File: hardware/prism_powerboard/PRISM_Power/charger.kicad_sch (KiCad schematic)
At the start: 23 parts, among them Q1 AO3400A, Q2 AO3400A, U2 BQ25895RTW, U3 BQ297xy

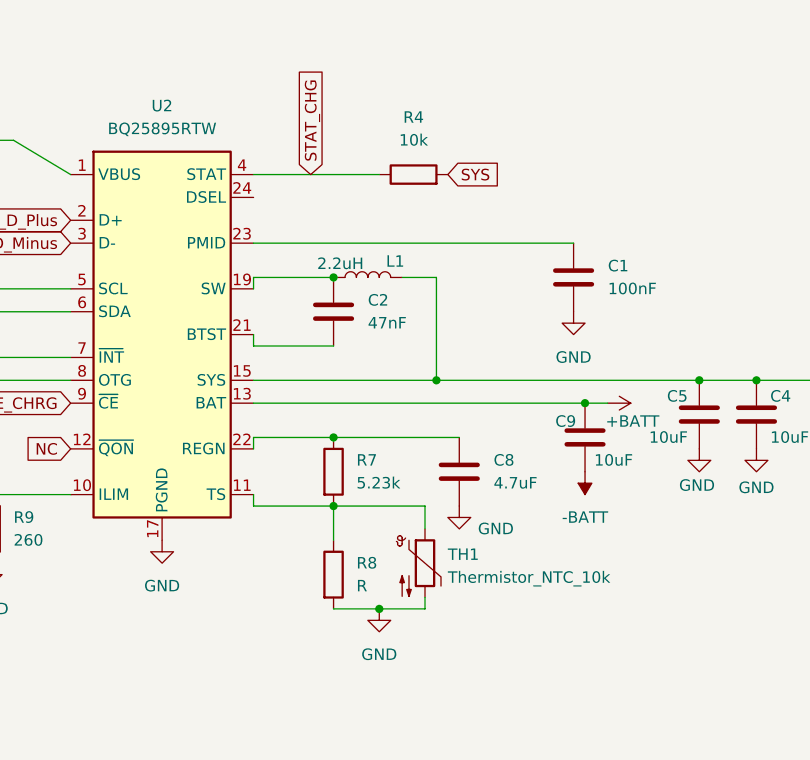
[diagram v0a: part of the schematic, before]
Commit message: Finished Schematics and Start Routing
Finished Schematics and started routing the PCB lines. Added and ensured all footprints were accurate
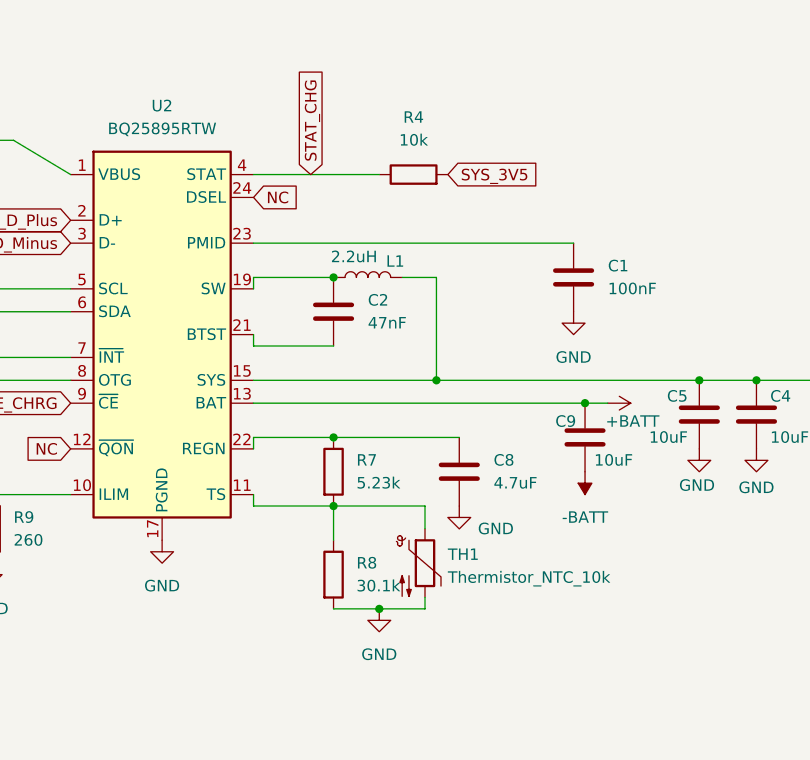
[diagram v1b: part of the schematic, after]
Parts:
- C1, C2, C3, C4, C5, C6, C8, C9: footprint (none) -> Capacitor_SMD:C_0805_2012Metric_Pad1.18x1.45mm_HandSolder
- L1: footprint (none) -> Inductor_SMD:L_0805_2012Metric_Pad1.05x1.20mm_HandSolder
- R10, R11, R2, R4, R5, R6, R7, R9: footprint (none) -> Resistor_SMD:R_0805_2012Metric_Pad1.20x1.40mm_HandSolder
- R8: value R -> 30.1k; footprint (none) -> Resistor_SMD:R_0805_2012Metric_Pad1.20x1.40mm_HandSolder
- TH1: footprint (none) -> Resistor_THT:R_Axial_DIN0204_L3.6mm_D1.6mm_P2.54mm_Vertical
- U2: footprint Package_DFN_QFN:Texas_RTW_WQFN-24-1EP_4x4mm_P0.5mm_EP2.7x2.7mm_ThermalVias -> BQ25895:RTW0024H
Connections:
- net NC: now also U2.24 (DSEL)
- net SYS: no longer R4.2
- new net SYS_3V5: R4.2
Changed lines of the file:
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@@
 		)
 	)
+	(global_label "NC"
+		(shape input)
+		(at 142.24 78.74 0)
+		(fields_autoplaced yes)
+		(effects
+			(font
+				(size 1.27 1.27)
+			)
+			(justify left)
+		)
+		(property "Intersheetrefs" "${INTERSHEET_REFS}"
+			(at 147.8257 78.74 0)
+			(hide yes)
+			(show_name no)
+			(do_not_autoplace no)
+			(effects
+				(font
+					(size 1.27 1.27)
+				)
+				(justify left)
+			)
+		)
+	)
 	(global_label "I2C_SCL_1V8"
 		(shape input)
@@
 		)
 	)
-	(global_label "SYS"
+	(global_label "SYS_3V5"
 		(shape input)
 		(at 163.83 76.2 0)
@@
 		)
 		(property "Intersheetrefs" "${INTERSHEET_REFS}"
-			(at 170.3228 76.2 0)
+			(at 174.798 76.2 0)
 			(hide yes)
 			(show_name no)
@@
 			)
 		)
-		(property "Footprint" ""
+		(property "Footprint" "Capacitor_SMD:C_0805_2012Metric_Pad1.18x1.45mm_HandSolder"
 			(at 39.0652 157.48 0)
 			(hide yes)
@@
 			)
 		)
-		(property "Footprint" ""
+		(property "Footprint" "Resistor_SMD:R_0805_2012Metric_Pad1.20x1.40mm_HandSolder"
 			(at 149.352 109.22 90)
 			(hide yes)
@@
 			)
 		)
-		(property "Footprint" ""
+		(property "Footprint" "Resistor_SMD:R_0805_2012Metric_Pad1.20x1.40mm_HandSolder"
 			(at 160.02 77.978 90)
 			(hide yes)
@@
 			)
 		)
-		(property "Footprint" ""
+		(property "Footprint" "Resistor_SMD:R_0805_2012Metric_Pad1.20x1.40mm_HandSolder"
 			(at 111.252 115.57 90)
 			(hide yes)
@@
 			)
 		)
-		(property "Footprint" ""
+		(property "Footprint" "Capacitor_SMD:C_0805_2012Metric_Pad1.18x1.45mm_HandSolder"
 			(at 107.6452 72.39 0)
 			(hide yes)
@@
 			)
 		)
-		(property "Footprint" ""
+		(property "Footprint" "Capacitor_SMD:C_0805_2012Metric_Pad1.18x1.45mm_HandSolder"
 			(at 199.0852 106.68 0)
 			(hide yes)
@@
 			)
 		)
-		(property "Footprint" ""
+		(property "Footprint" "Resistor_SMD:R_0805_2012Metric_Pad1.20x1.40mm_HandSolder"
 			(at 53.34 150.368 90)
 			(hide yes)
@@
 			)
 		)
-		(property "Footprint" ""
+		(property "Footprint" "Capacitor_SMD:C_0805_2012Metric_Pad1.18x1.45mm_HandSolder"
 			(at 176.8348 83.82 0)
 			(hide yes)
@@
 			)
 		)
-		(property "Footprint" ""
+		(property "Footprint" "Capacitor_SMD:C_0805_2012Metric_Pad1.18x1.45mm_HandSolder"
 			(at 192.7352 106.68 0)
 			(hide yes)
@@
 		)
 		(property "Value" "2.2uH"
-			(at 151.892 86.106 90)
+			(at 153.416 85.344 90)
 			(show_name no)
 			(do_not_autoplace no)
@@
 			)
 		)
-		(property "Footprint" ""
+		(property "Footprint" "Inductor_SMD:L_0805_2012Metric_Pad1.05x1.20mm_HandSolder"
 			(at 154.94 87.63 0)
 			(hide yes)
@@
 			)
 		)
-		(property "Footprint" ""
+		(property "Footprint" "Resistor_SMD:R_0805_2012Metric_Pad1.20x1.40mm_HandSolder"
 			(at 100.838 85.09 90)
 			(hide yes)
@@
 			)
 		)
-		(property "Footprint" ""
+		(property "Footprint" "Capacitor_SMD:C_0805_2012Metric_Pad1.18x1.45mm_HandSolder"
 			(at 150.1648 87.63 0)
 			(hide yes)
@@
 			)
 		)
-		(property "Footprint" ""
+		(property "Footprint" "Resistor_SMD:R_0805_2012Metric_Pad1.20x1.40mm_HandSolder"
 			(at 95.758 87.63 90)
 			(hide yes)
@@
 			)
 		)
-		(property "Footprint" ""
+		(property "Footprint" "Resistor_THT:R_Axial_DIN0204_L3.6mm_D1.6mm_P2.54mm_Vertical"
 			(at 161.29 118.11 0)
 			(hide yes)
@@
 			)
 		)
-		(property "Footprint" "Package_DFN_QFN:Texas_RTW_WQFN-24-1EP_4x4mm_P0.5mm_EP2.7x2.7mm_ThermalVias"
+		(property "Footprint" "BQ25895:RTW0024H"
 			(at 132.08 123.444 0)
 			(hide yes)
@@
 			)
 		)
-		(property "Footprint" ""
+		(property "Footprint" "Capacitor_SMD:C_0805_2012Metric_Pad1.18x1.45mm_HandSolder"
 			(at 166.0652 113.03 0)
 			(hide yes)
@@
 			)
 		)
-		(property "Footprint" ""
+		(property "Footprint" "Capacitor_SMD:C_0805_2012Metric_Pad1.18x1.45mm_HandSolder"
 			(at 180.0352 109.22 0)
 			(hide yes)
@@
 			)
 		)
-		(property "Footprint" ""
+		(property "Footprint" "Resistor_SMD:R_0805_2012Metric_Pad1.20x1.40mm_HandSolder"
 			(at 89.408 100.33 90)
 			(hide yes)
@@
 			)
 		)
-		(property "Footprint" ""
+		(property "Footprint" "Resistor_SMD:R_0805_2012Metric_Pad1.20x1.40mm_HandSolder"
 			(at 46.482 157.48 90)
 			(hide yes)
@@
 			)
 		)
-		(property "Value" "R"
+		(property "Value" "30.1k"
 			(at 153.67 121.9199 0)
 			(show_name no)
@@
 			)
 		)
-		(property "Footprint" ""
+		(property "Footprint" "Resistor_SMD:R_0805_2012Metric_Pad1.20x1.40mm_HandSolder"
 			(at 149.352 120.65 90)
 			(hide yes)

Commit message: Routing Updates
Nearly finished with Power Board PCB. Highly unoptimized and removed some pieces. Still need to ensure all needed connections are available.
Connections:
- net SYS is gone; now on net SYS_3V5: C4.1, C5.1, L1.2, U2.15 (SYS), U2.16 (SYS)
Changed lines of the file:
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@@
+		)
+	)
+	(global_label "SYS_3V5"
+		(shape input)
+		(at 204.47 99.06 0)
+		(fields_autoplaced yes)
+		(effects
+			(font
+				(size 1.27 1.27)
+			)
+			(justify left)
+		)
+		(property "Intersheetrefs" "${INTERSHEET_REFS}"
+			(at 215.438 99.06 0)
+			(hide yes)
+			(show_name no)
+			(do_not_autoplace no)
+			(effects
+				(font
+					(size 1.27 1.27)
+				)
+				(justify left)
+			)
 		)
 	)
@@
 			)
 		)
-	)
-	(global_label "SYS"
-		(shape input)
-		(at 204.47 99.06 0)
-		(fields_autoplaced yes)
-		(effects
-			(font
-				(size 1.27 1.27)
-			)
-			(justify left)
-		)
-		(property "Intersheetrefs" "${INTERSHEET_REFS}"
-			(at 210.9628 99.06 0)
-			(hide yes)
-			(show_name no)
-			(do_not_autoplace no)
-			(effects
-				(font
-					(size 1.27 1.27)
-				)
-				(justify left)
-			)
-		)
